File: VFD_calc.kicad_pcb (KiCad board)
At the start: 2 copper layers, 148.6 x 180.3 mm, 192 parts, among them CON1 AVR-ISP-6, J1 Conn_01x02_Female, J2 USB_OTG, J3 Conn_01x05, K1 RES-60, Q1 2N2222, Q10 MP26, Q11 2N2222, Q12 MP26, Q13 2N2222, Q14 MP26, Q15 BSS83P, Q16 BC817, Q17 BC817, Q18 BC856, Q19 BC817, Q2 MP26, Q20 BC856, Q21 BC817, Q22 BC856, Q23 BC817, Q24 BC856, Q25 BC817, Q26 BC856, Q27 BC817, Q28 BC856, Q29 BC817, Q3 2N2222, Q30 BC856, Q31 BC817, Q32 BC856, Q33 BC817, Q34 BC856, Q35 BC817, Q36 BC856, Q37 BC817, Q38 BC856, Q39 BC817, Q4 MP26, Q40 BC856, Q41 BC817, Q42 BC856, Q43 BC817, Q44 BC856, Q45 BC817, Q46 BC856, Q47 BC817, Q48 BC856, Q49 BC856, Q5 2N2222, Q50 BC817, Q51 BC856, Q6 MP26, Q7 2N2222, Q8 MP26, Q9 2N2222, SW1 SW_Push, SW10 SW_Push_45deg, SW11 SW_Push_45deg, SW12 SW_Push_45deg, SW13 SW_Push_45deg, SW14 SW_Push_45deg, SW15 SW_Push_45deg, SW16 SW_Push_45deg, SW17 SW_Push_45deg, SW18 SW_Push_45deg, SW19 SW_Push_45deg, SW2 SW_Push_45deg, SW3 SW_Push_45deg, SW4 SW_Push_45deg, SW5 SW_Push_45deg, SW6 SW_Push_45deg, SW7 SW_Push_45deg, SW8 SW_Push_45deg, SW9 SW_Push_45deg, U1 ATMEGA328P-AU

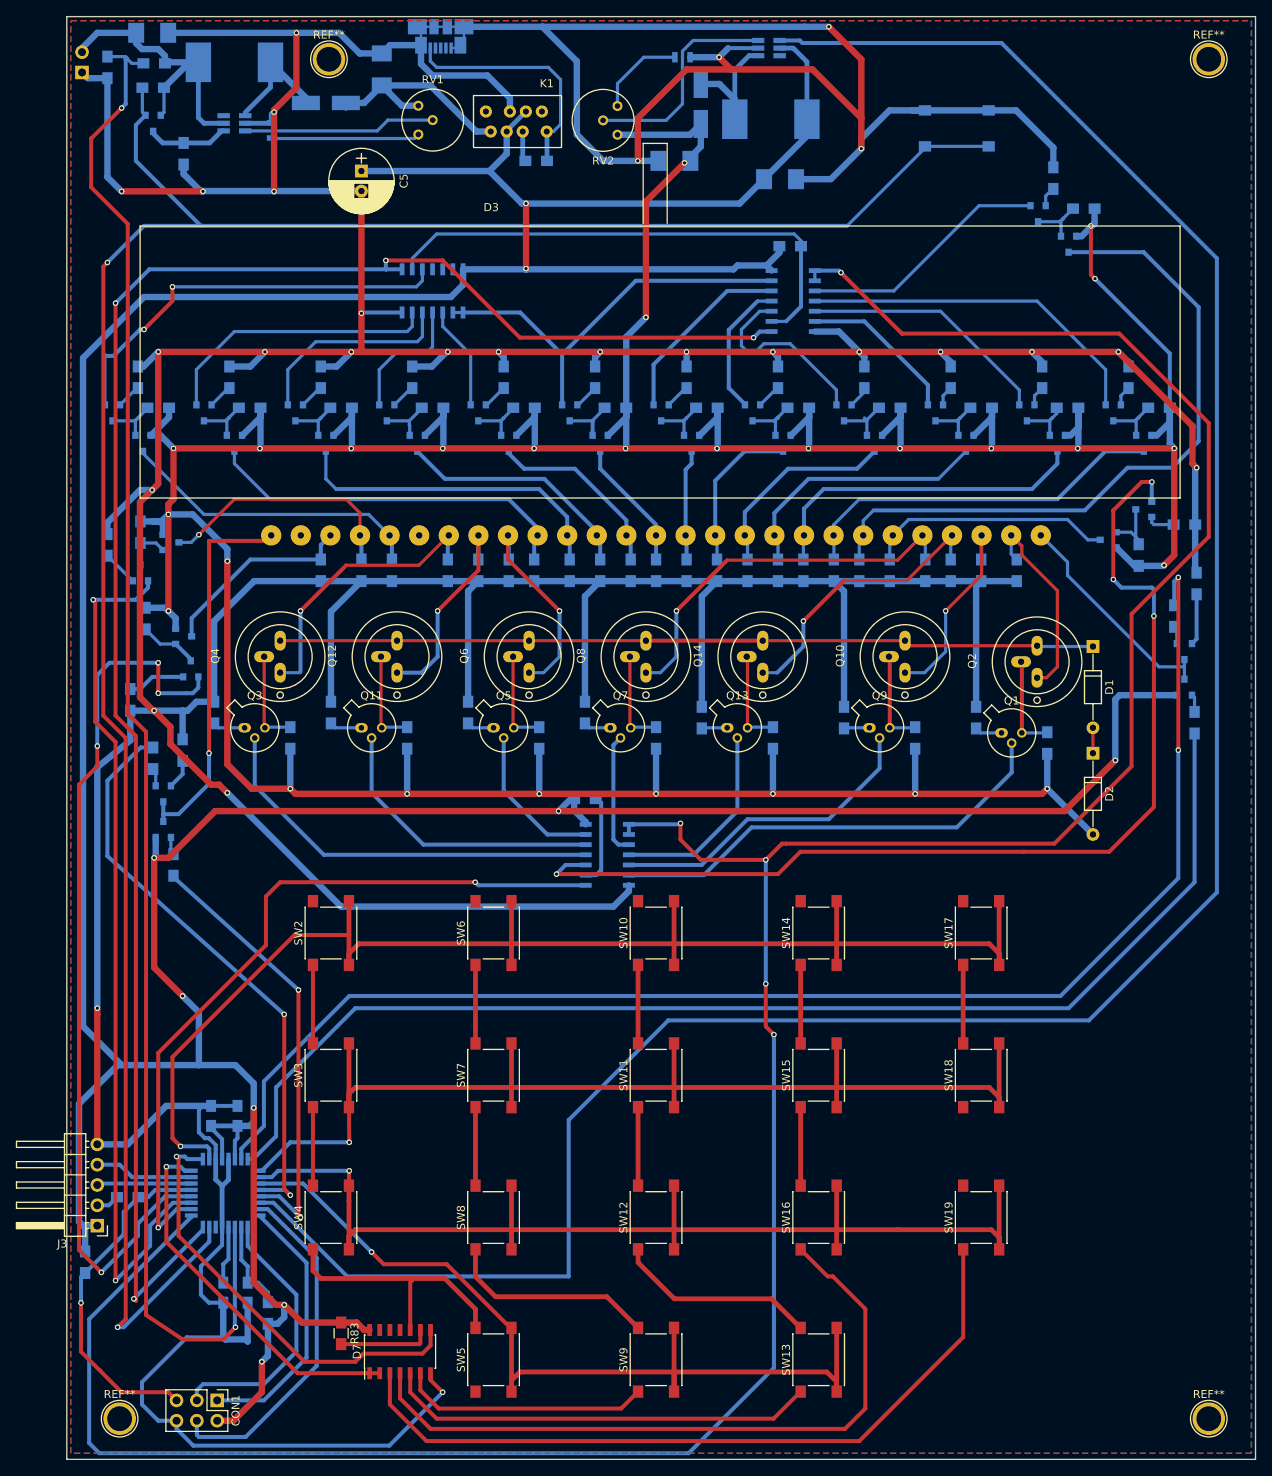
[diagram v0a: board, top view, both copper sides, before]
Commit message: Modified board layout (stil awful), so now it is more compact
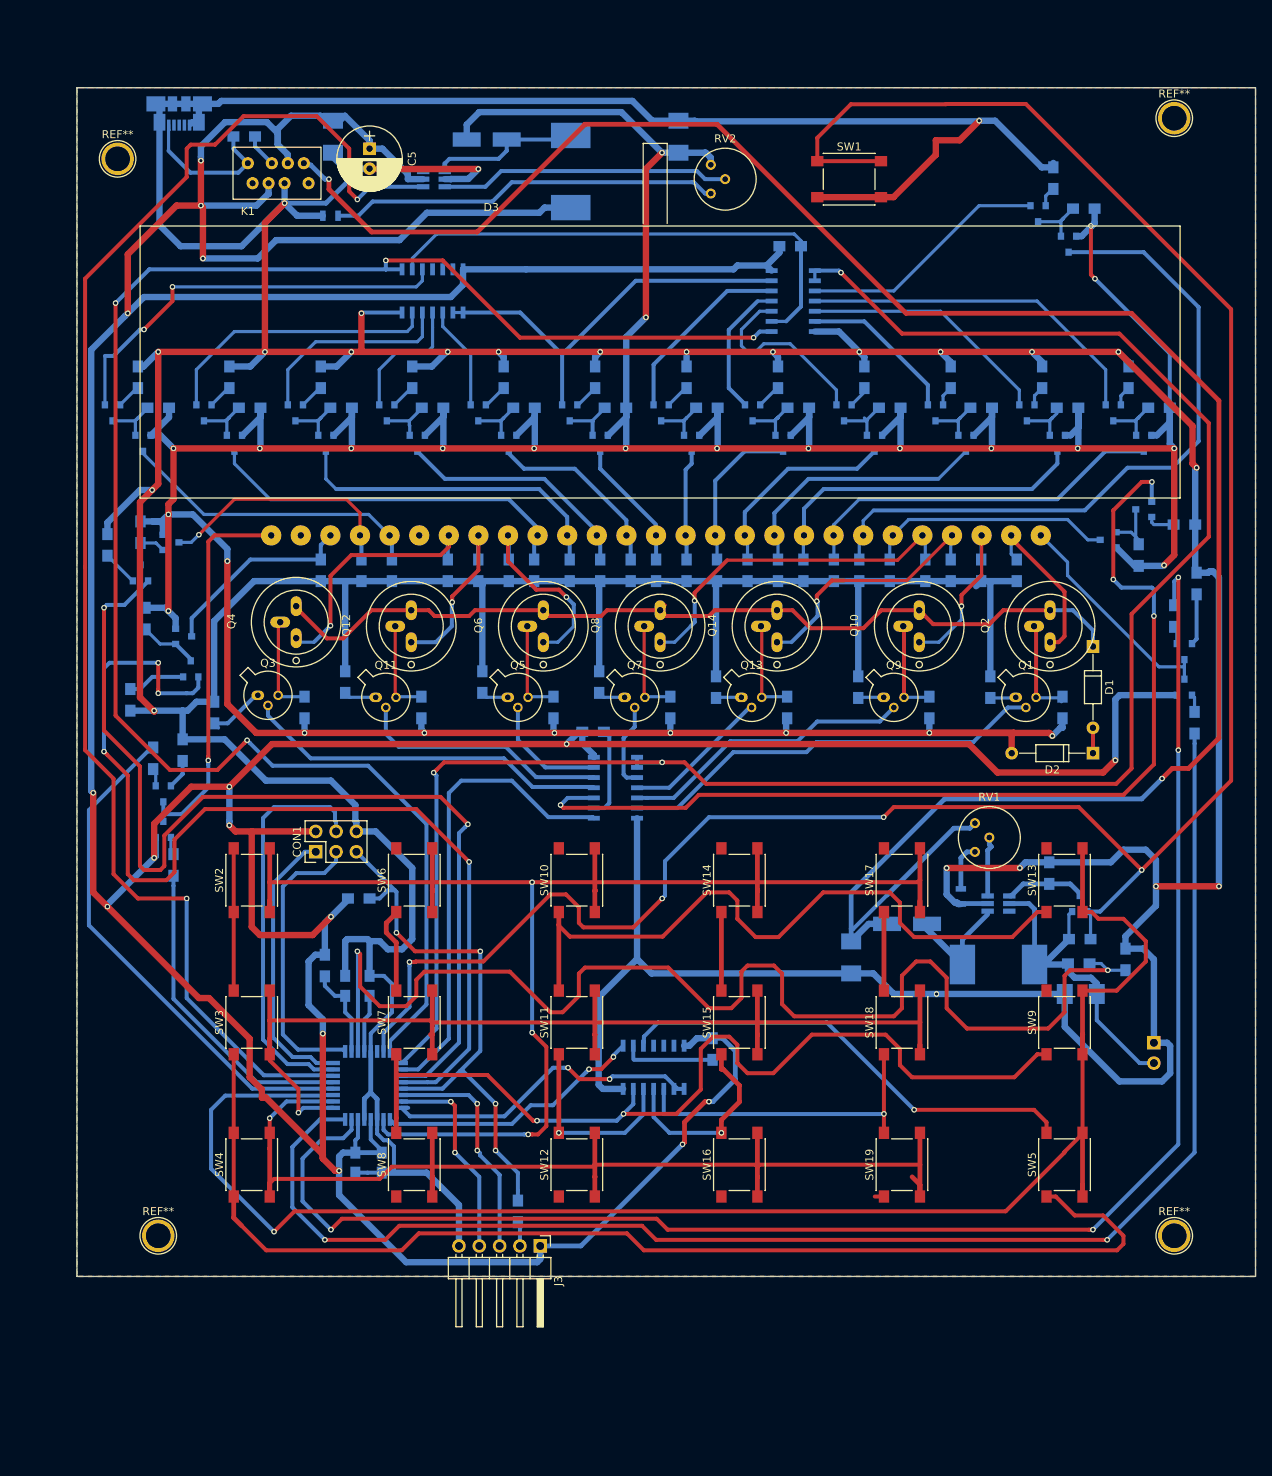
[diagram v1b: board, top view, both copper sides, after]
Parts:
- D7, R83: moved to B.Cu
- SW1: moved to F.Cu
- moved J1 180.7 mm to (162.6, 143.5), turned to 180 degrees
- moved R23 169.2 mm to (159.0, 133.1), turned to 90 degrees
- moved C7 167.1 mm to (153.4, 137.4), turned to 180 degrees
- moved R22 161.3 mm to (153.2, 133.6), turned to 0 degrees
- moved R24 157.3 mm to (153.3, 130.6), turned to 0 degrees
- moved Q15 151.4 mm to (153.3, 126.1), turned to 90 degrees
- moved L1 147.8 mm to (143.1, 133.7), turned to 180 degrees
- moved R73 140.7 mm to (149.5, 122.3), turned to 90 degrees
- moved D8 136.5 mm to (143.1, 126.1), turned to 0 degrees
- moved R84 128.8 mm to (138.4, 125.2), turned to 270 degrees
- moved D9 125.7 mm to (131.7, 128.7), turned to 0 degrees
- moved C8 125.6 mm to (124.7, 132.8), turned to 270 degrees
- moved RV1 113.5 mm to (140.2, 119.7)
- moved SW5 75.4 mm to (151.4, 158.8)
- moved CON1 69.7 mm to (57.8, 119.6), turned to 90 degrees
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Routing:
- net /Step UP/VOUT: track 28.3 -> 270.0 mm, vias 0 -> 2
- net Net-(D7-Pad10): track 54.0 -> 224.6 mm, vias 0 -> 1
- net DISPL_DATA: track 365.9 -> 238.2 mm, vias 5 -> 3
- net HV_EN: track 300.0 -> 182.0 mm, vias 0 -> 2
- net +5V: track 579.7 -> 678.1 mm, vias 9 -> 16
- net /Matrix keypad/ROW_4: track 109.6 -> 201.2 mm
- net Net-(D7-Pad4): track 107.2 -> 34.4 mm, vias 0 -> 1
- net Net-(D7-Pad6): track 77.2 -> 130.5 mm, vias 0 -> 2
- net Net-(D7-Pad3): track 103.6 -> 51.5 mm, vias 0 -> 1
- net Net-(R22-Pad2): track 192.3 -> 153.1 mm
- net Net-(R85-Pad1): track 11.4 -> 48.9 mm
- net SEG_CLK: track 92.9 -> 58.9 mm, vias 2 -> 0
- net B_H: track 154.9 -> 188.4 mm, vias 0 -> 2
- net B_L: track 177.0 -> 205.3 mm, vias 2 -> 4
- net PC6: track 44.1 -> 70.9 mm, vias 1 -> 4
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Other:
- board size 148.6 x 180.3 mm -> 147.3 x 148.6 mm

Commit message: Increased vias, generated pdfs
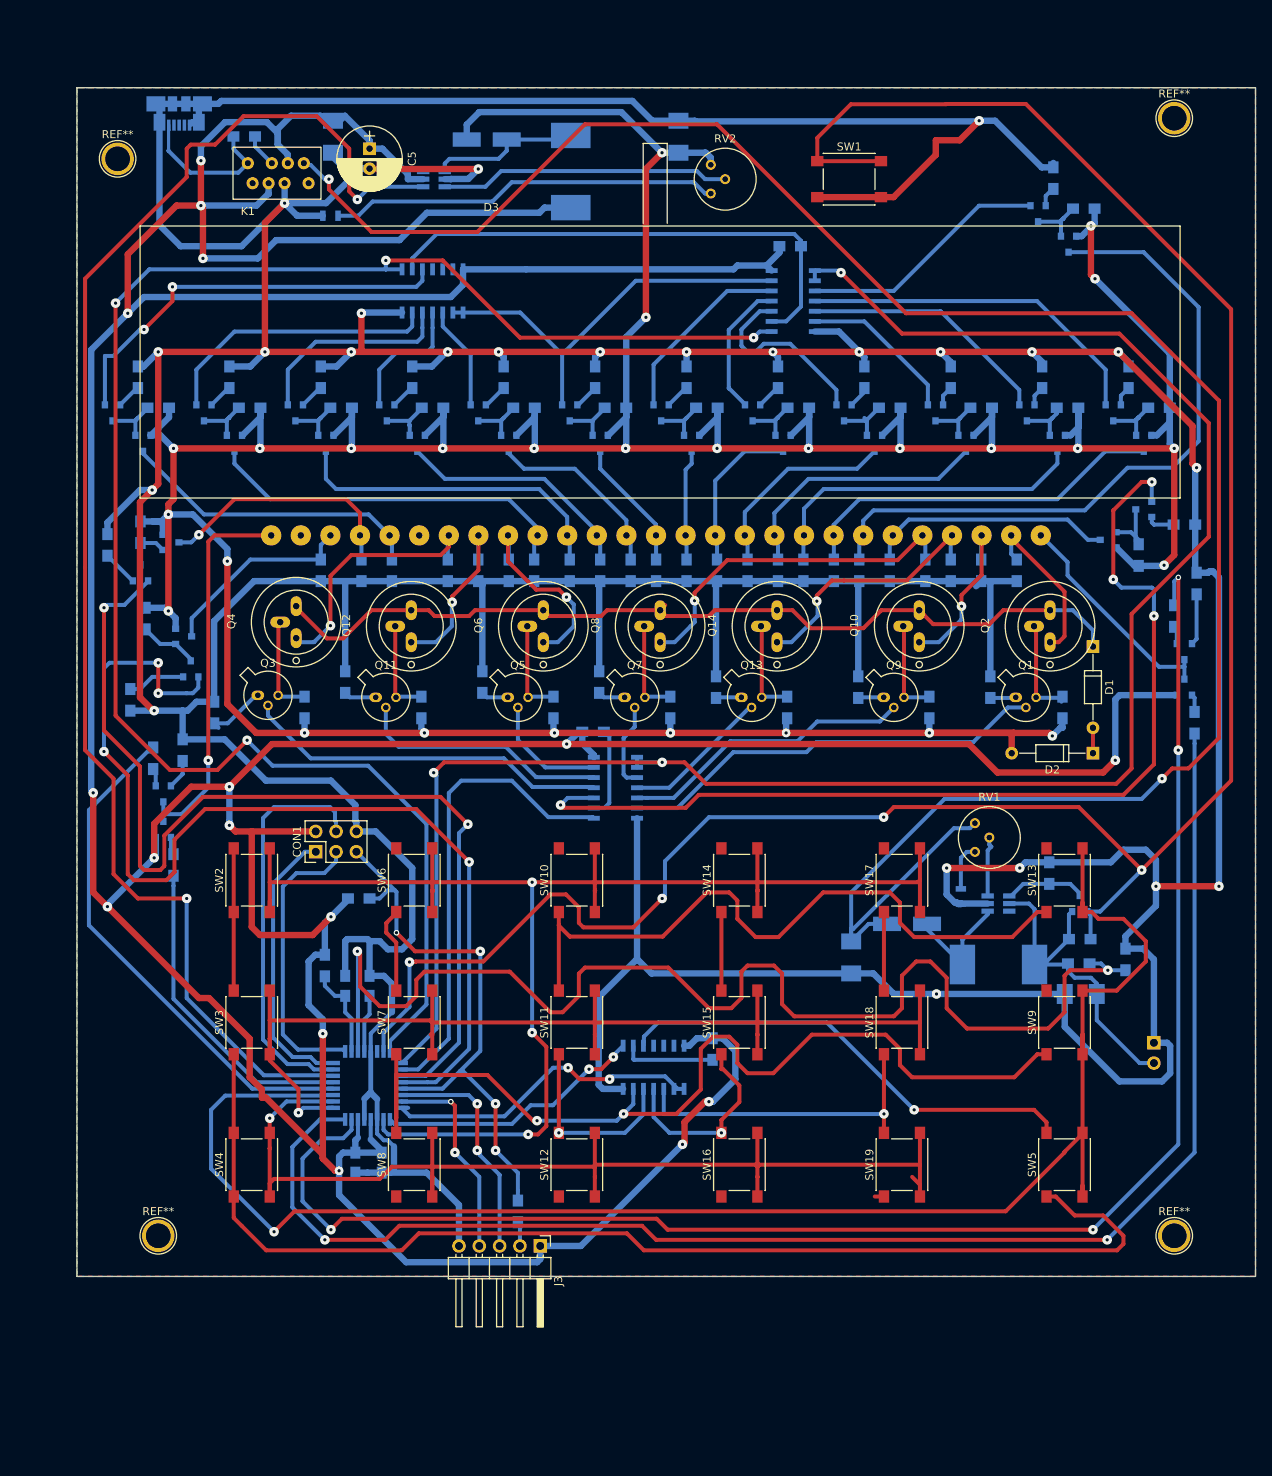
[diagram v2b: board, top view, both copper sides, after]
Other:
- net class Default: via_dia 0.7 -> 1.2
- net class Power: via_dia 0.7 -> 1.2
